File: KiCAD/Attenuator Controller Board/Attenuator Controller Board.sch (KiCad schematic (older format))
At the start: 33 parts, among them J1 Barrel_Jack_Switch, J2 Conn_Coaxial, J3 Conn_Coaxial, J4 Conn_01x24_Female, J5 DSub_15_HD, J6 DSub9, J7 DSub9, J8 DSub9, J9 Conn_01x24_Female, U1 ADM3307EARUZ, U2 ZXMHC3A01T8TA, U3 Teensy3.6

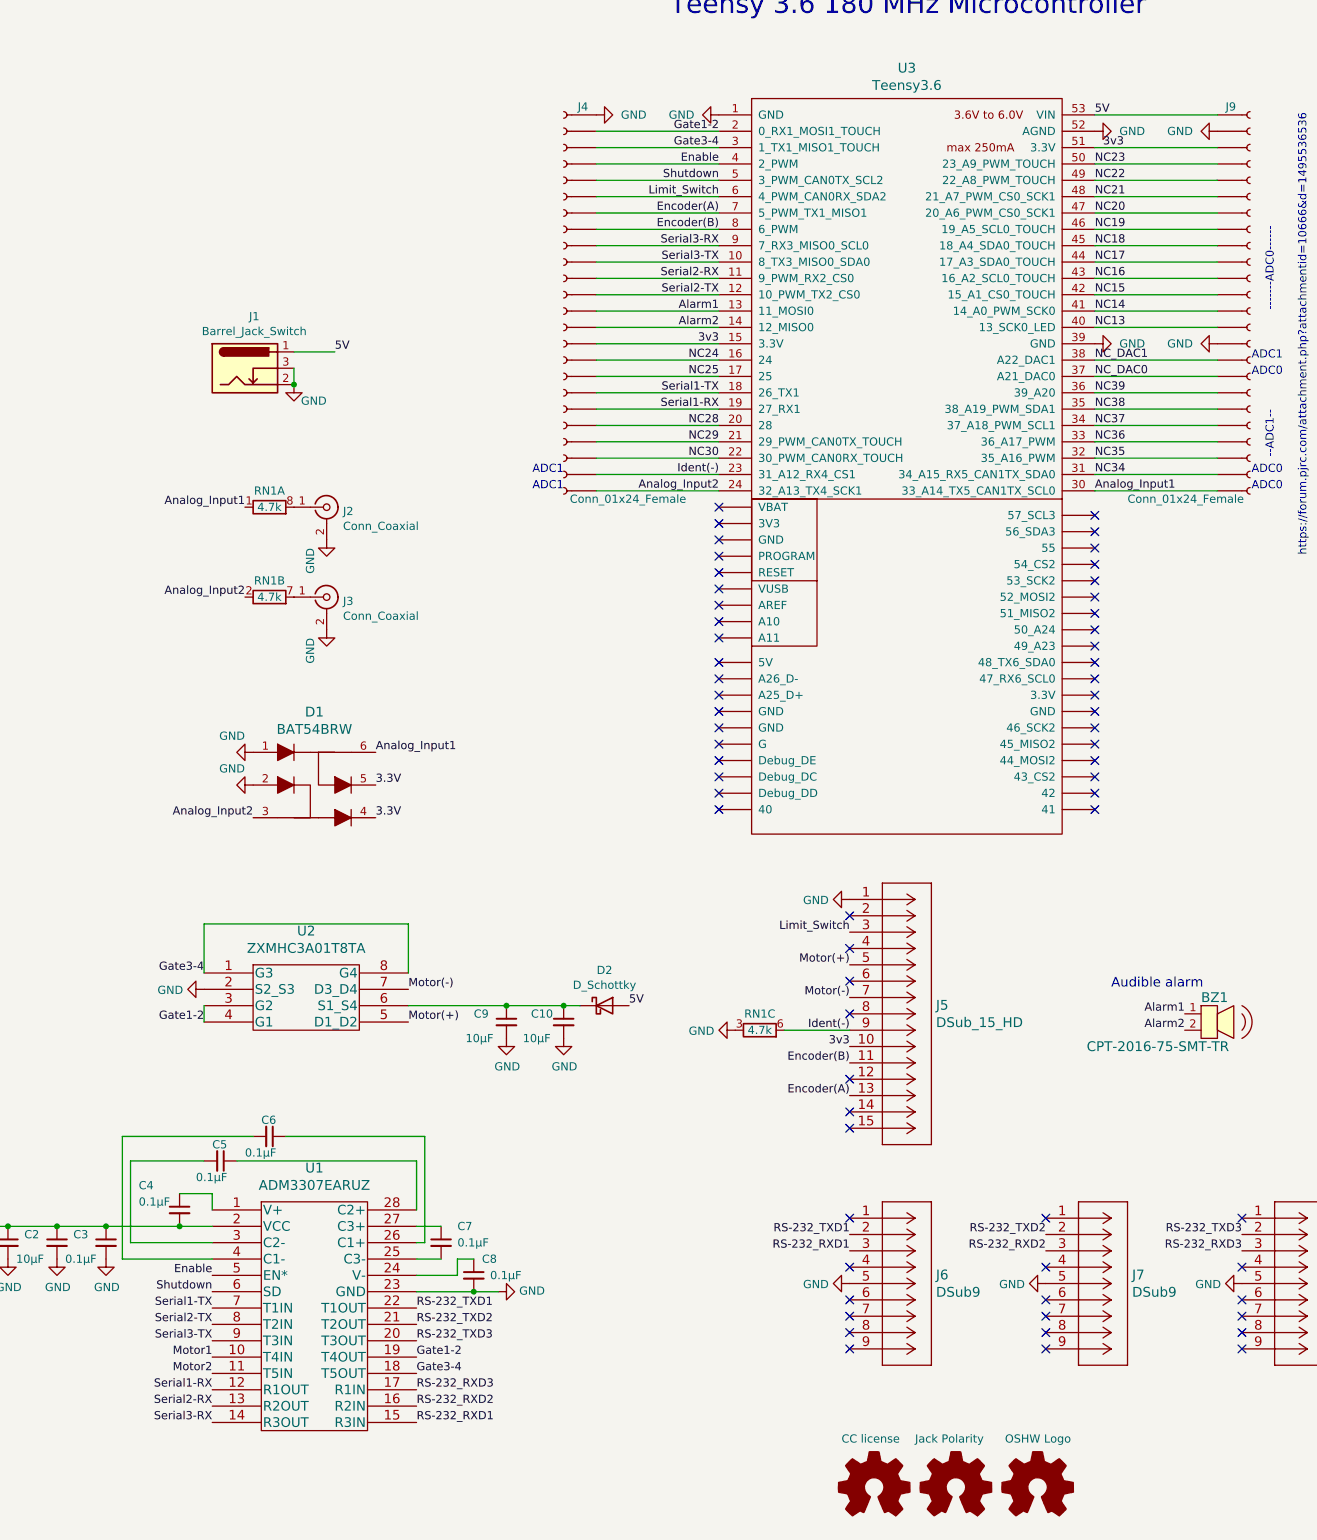
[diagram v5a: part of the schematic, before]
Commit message: Keep SD and EN low to keep RS-232 driver always on
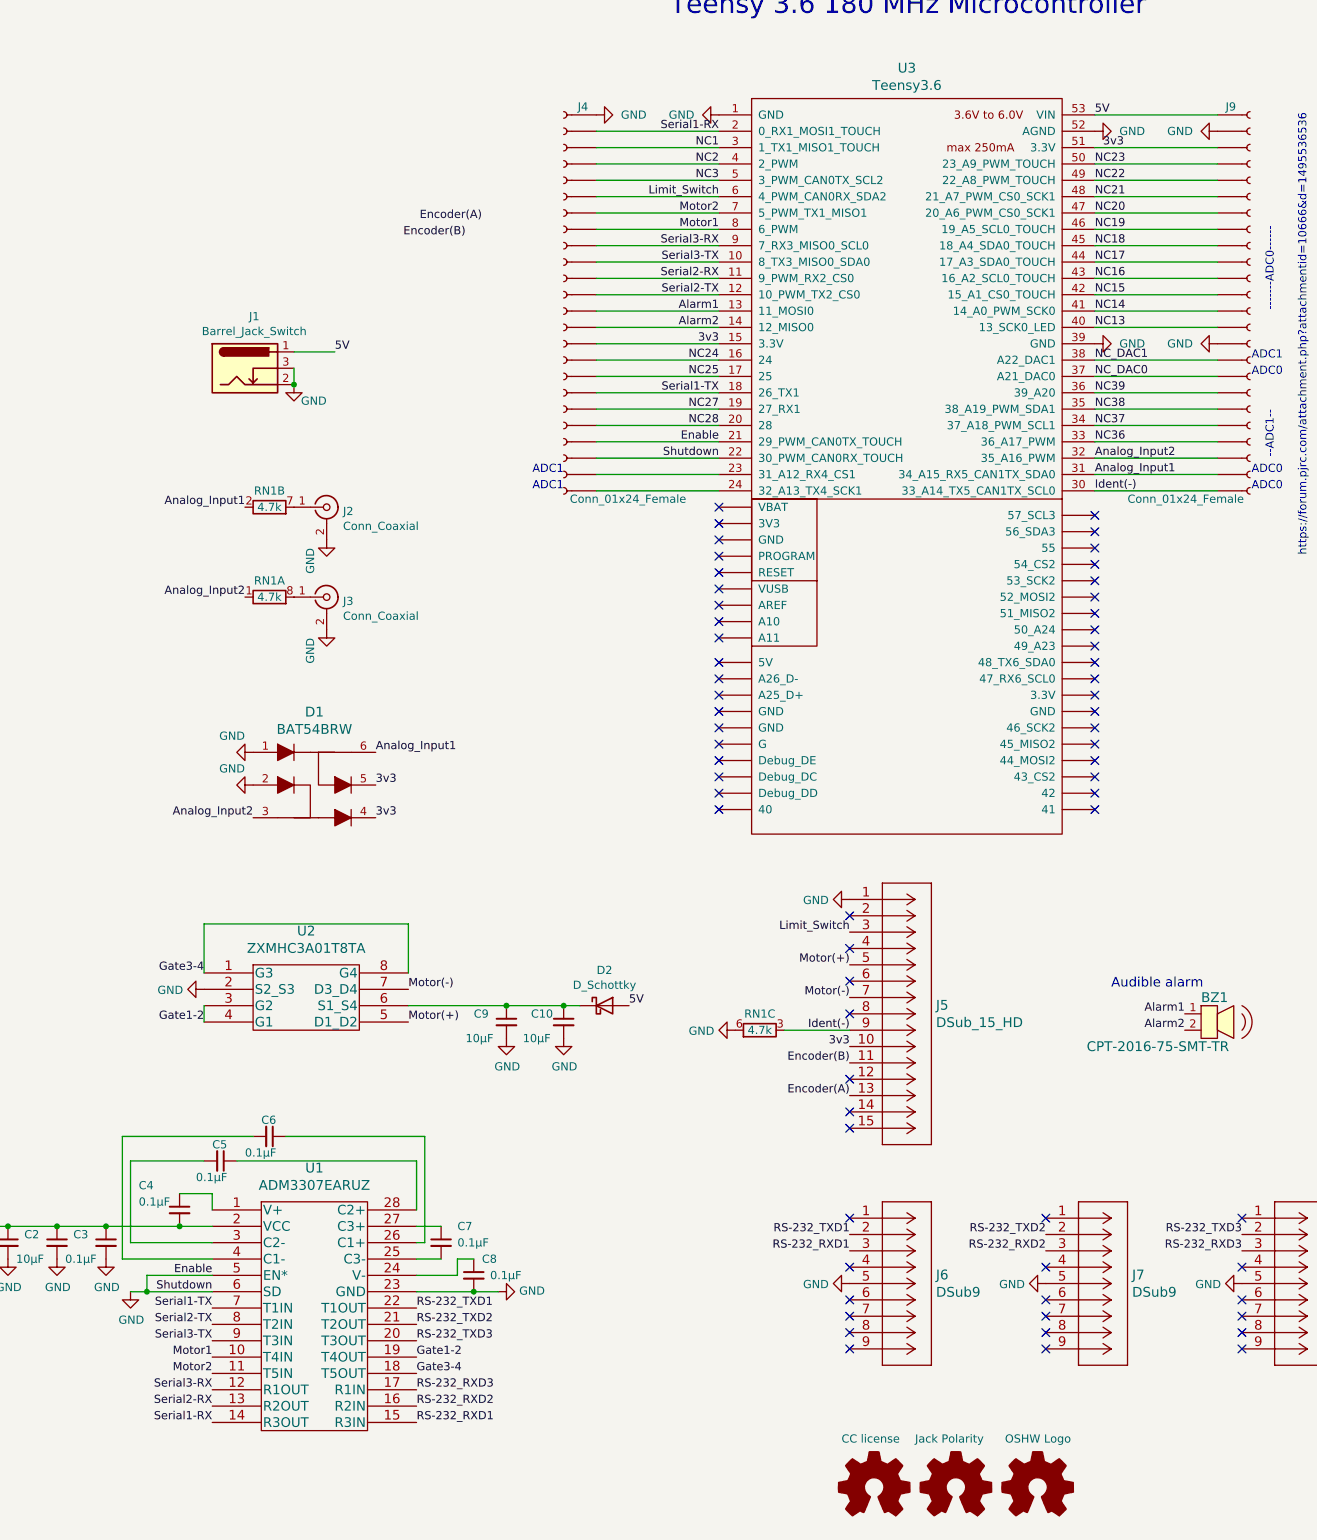
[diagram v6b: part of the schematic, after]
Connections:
- net 3.3V is gone; now on net 3v3: D1.4, D1.5
- net Analog_Input1: now also RN1.2 (R2.1), U3.31 (34_A15_RX5_CAN1TX_SDA0); no longer RN1.1 (R1.1), U3.30 (33_A14_TX5_CAN1TX_SCL0)
- net Analog_Input2: now also J9.~, RN1.1 (R1.1), U3.32 (35_A16_PWM); no longer J4.~, RN1.2 (R2.1), U3.24 (32_A13_TX4_SCK1)
- net Encoder(A): no longer J4.~, U3.7 (5_PWM_TX1_MISO1)
- net Encoder(B): no longer J4.~, U3.8 (6_PWM)
- net GND: now also RN1.6 (R3.2), U1.5 (EN*), U1.6 (SD), U3.21 (29_PWM_CAN0TX_TOUCH), U3.22 (30_PWM_CAN0RX_TOUCH); no longer RN1.3 (R3.1)
- net Gate1-2: no longer J4.~, U3.2 (0_RX1_MOSI1_TOUCH)
- net Gate3-4: no longer J4.~, U3.3 (1_TX1_MISO1_TOUCH)
- net Ident(-): now also J9.~, RN1.3 (R3.1), U3.30 (33_A14_TX5_CAN1TX_SCL0); no longer J4.~, RN1.6 (R3.2), U3.23 (31_A12_RX4_CS1)
- net Motor1: now also J4.~, U3.8 (6_PWM)
- net Motor2: now also J4.~, U3.7 (5_PWM_TX1_MISO1)
- net Serial1-RX: now also U1.14 (R3OUT), U3.2 (0_RX1_MOSI1_TOUCH); no longer U1.12 (R1OUT), U3.19 (27_RX1)
- net Serial3-RX: now also U1.12 (R1OUT); no longer U1.14 (R3OUT)
- net at J2.1 (In): now also RN1.7 (R2.2); no longer RN1.8 (R1.2)
- net at J3.1 (In): now also RN1.8 (R1.2); no longer RN1.7 (R2.2)
- removed net Enable: J4.~, U1.5 (EN*), U3.4 (2_PWM)
- removed net NC29: J4.~, U3.21 (29_PWM_CAN0TX_TOUCH)
- removed net NC30: J4.~, U3.22 (30_PWM_CAN0RX_TOUCH)
- removed net NC34: J9.~, U3.31 (34_A15_RX5_CAN1TX_SDA0)
- removed net NC35: J9.~, U3.32 (35_A16_PWM)
- removed net Shutdown: J4.~, U1.6 (SD), U3.5 (3_PWM_CAN0TX_SCL2)
- new net: J4.~, U3.23 (31_A12_RX4_CS1)
- new net: J4.~, U3.24 (32_A13_TX4_SCK1)
- new net NC1: J4.~, U3.3 (1_TX1_MISO1_TOUCH)
- new net NC2: J4.~, U3.4 (2_PWM)
- new net NC27: J4.~, U3.19 (27_RX1)
- new net NC3: J4.~, U3.5 (3_PWM_CAN0TX_SCL2)
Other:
- moved on the sheet: RN1A, RN1B
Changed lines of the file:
@@
 Text Label 13850 1500 0    50   ~ 0
 3v3
-Text Label 11500 3100 2    50   ~ 0
-Serial1-RX
 Text Label 11500 3000 2    50   ~ 0
 Serial1-TX
@@
 Text Label 8400 8600 2    50   ~ 0
 Serial1-TX
-Text Label 8400 9100 2    50   ~ 0
+Text Label 8400 9300 2    50   ~ 0
 Serial1-RX
 Text Label 11500 2300 2    50   ~ 0
@@
 Text Label 10950 6750 0    50   ~ 0
 5V
-Text Label 11500 1400 2    50   ~ 0
-Gate1-2
-Text Label 11500 1500 2    50   ~ 0
-Gate3-4
 Text Label 8350 6850 2    50   ~ 0
 Gate1-2
@@
 Text Label 9650 9100 0    50   ~ 0
 RS-232_RXD3
-Text Label 8400 9300 2    50   ~ 0
+Text Label 8400 9100 2    50   ~ 0
 Serial3-RX
 NoConn ~ 14700 8850
@@
 Text Label 8400 8500 2    50   ~ 0
 Shutdown
-Text Label 11500 1600 2    50   ~ 0
+Text Label 11500 3300 2    50   ~ 0
 Enable
-Text Label 11500 1700 2    50   ~ 0
+Text Label 11500 3400 2    50   ~ 0
 Shutdown
 Text Label 11500 1800 2    50   ~ 0
 Limit_Switch
-Text Label 11500 1900 2    50   ~ 0
+Text Label 10050 1950 2    50   ~ 0
 Encoder(A)
-Text Label 11500 2000 2    50   ~ 0
+Text Label 9950 2050 2    50   ~ 0
 Encoder(B)
 Text Label 12300 6500 2    50   ~ 0
@@
 	0    1    1    0
 $EndComp
-Text Label 11500 3500 2    50   ~ 0
+Text Label 13800 3600 0    50   ~ 0
 Ident(-)
 $Comp
@@
 $EndComp
 Text Label 9400 5400 0    50   ~ 0
-3.3V
+3v3
 Wire Wire Line
 	8900 2850 8900 2950
@@
 5V
 Text Label 9400 5600 0    50   ~ 0
-3.3V
+3v3
 $Comp
 L power:GND #PWR06
@@
 Text Label 8650 5600 2    50   ~ 0
 Analog_Input2
-Text Label 13800 3600 0    50   ~ 0
+Text Label 13800 3500 0    50   ~ 0
 Analog_Input1
-Text Label 11500 3600 2    50   ~ 0
+Text Label 13800 3400 0    50   ~ 0
 Analog_Input2
 $Comp
@@
 L Device:R_Pack04_Split RN1
 U 1 1 61FBFC7D
+P 8750 4250
+F 0 "RN1" V 8650 4250 50  0000 C CNN
+F 1 "4.7k" V 8750 4250 50  0000 C CNN
+F 2 "Resistor_SMD:R_Array_Convex_4x1206" V 8670 4250 50  0001 C CNN
+F 3 "https://industrial.panasonic.com/cdbs/www-data/pdf/AOC0000/AOC0000C14.pdf" H 8750 4250 50  0001 C CNN
+F 4 "Panasonic Electronic Components" V 8750 4250 50  0001 C CNN "Manufacturer"
+F 5 "EXB-38V472JV" V 8750 4250 50  0001 C CNN "Part #"
+	1    8750 4250
+	0    1    1    0
+$EndComp
+$Comp
+L Device:R_Pack04_Split RN1
+U 2 1 61FC4641
 P 8750 3700
 F 0 "RN1" V 8650 3700 50  0000 C CNN
@@
 F 4 "Panasonic Electronic Components" V 8750 3700 50  0001 C CNN "Manufacturer"
 F 5 "EXB-38V472JV" V 8750 3700 50  0001 C CNN "Part #"
-	1    8750 3700
-	0    1    1    0
-$EndComp
-$Comp
-L Device:R_Pack04_Split RN1
-U 2 1 61FC4641
-P 8750 4250
-F 0 "RN1" V 8650 4250 50  0000 C CNN
-F 1 "4.7k" V 8750 4250 50  0000 C CNN
-F 2 "Resistor_SMD:R_Array_Convex_4x1206" V 8670 4250 50  0001 C CNN
-F 3 "https://industrial.panasonic.com/cdbs/www-data/pdf/AOC0000/AOC0000C14.pdf" H 8750 4250 50  0001 C CNN
-F 4 "Panasonic Electronic Components" V 8750 4250 50  0001 C CNN "Manufacturer"
-F 5 "EXB-38V472JV" V 8750 4250 50  0001 C CNN "Part #"
-	2    8750 4250
+	2    8750 3700
 	0    1    1    0
 $EndComp
@@
 F 5 "EXB-38V472JV" V 11750 6900 50  0001 C CNN "Part #"
 	3    11750 6900
-	0    1    1    0
+	0    -1   1    0
 $EndComp
 $Comp
@@
 Text Label 11500 3200 2    50   ~ 0
 NC28
-Text Label 11500 3300 2    50   ~ 0
-NC29
-Text Label 11500 3400 2    50   ~ 0
-NC30
 Text Label 13800 1600 0    50   ~ 0
 NC23
@@
 Text Label 13800 3300 0    50   ~ 0
 NC36
-Text Label 13800 3400 0    50   ~ 0
-NC35
-Text Label 13800 3500 0    50   ~ 0
-NC34
 $Comp
 L Device:C_Small C10
@@
 	1    0    0    -1
 $EndComp
+Text Label 11500 2000 2    50   ~ 0
+Motor1
+Text Label 11500 1900 2    50   ~ 0
+Motor2
+Text Label 11500 1400 2    50   ~ 0
+Serial1-RX
+Text Label 11500 3100 2    50   ~ 0
+NC27
+Text Label 11500 1500 2    50   ~ 0
+NC1
+Text Label 11500 1600 2    50   ~ 0
+NC2
+Text Label 11500 1700 2    50   ~ 0
+NC3
+Wire Wire Line
+	8400 8500 8000 8500
+Wire Wire Line
+	8400 8400 8000 8400
+Wire Wire Line
+	8000 8400 8000 8500
+$Comp
+L power:GND #PWR0103
+U 1 1 61E59326
+P 7900 8500
+F 0 "#PWR0103" H 7900 8250 50  0001 C CNN
+F 1 "GND" H 7905 8327 50  0000 C CNN
+F 2 "" H 7900 8500 50  0001 C CNN
+F 3 "" H 7900 8500 50  0001 C CNN
+	1    7900 8500
+	1    0    0    -1
+$EndComp
+Wire Wire Line
+	8000 8500 7900 8500
+Connection ~ 8000 8500
 $EndSCHEMATC

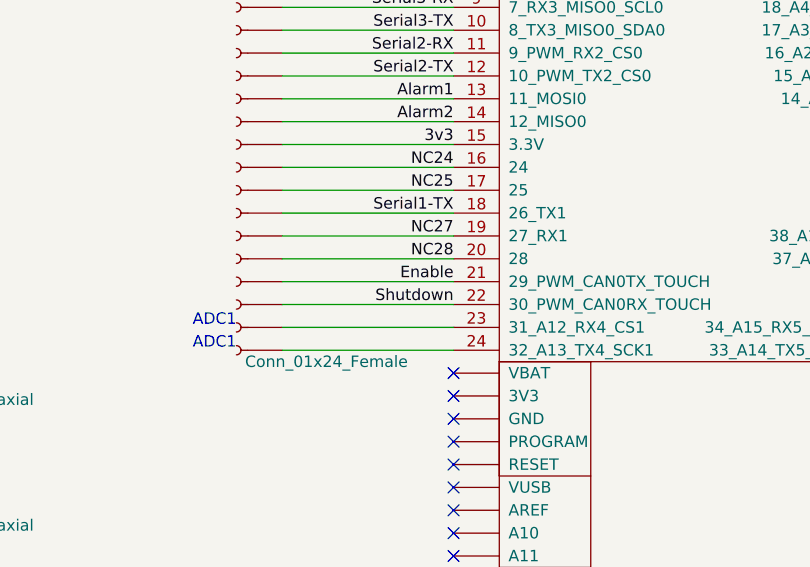
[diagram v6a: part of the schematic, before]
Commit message: Disconnect SD and EN from Teensy
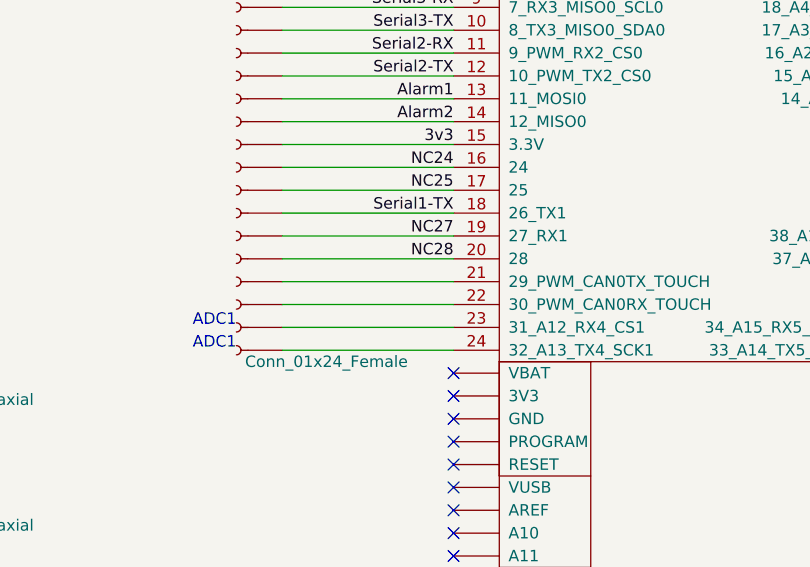
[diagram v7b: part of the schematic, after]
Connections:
- net GND: no longer U3.21 (29_PWM_CAN0TX_TOUCH), U3.22 (30_PWM_CAN0RX_TOUCH)
- new net: J4.~, U3.21 (29_PWM_CAN0TX_TOUCH)
- new net: J4.~, U3.22 (30_PWM_CAN0RX_TOUCH)
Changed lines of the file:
@@
 Text Label 8400 8500 2    50   ~ 0
-Shutdown
-Text Label 11500 3300 2    50   ~ 0
-Enable
-Text Label 11500 3400 2    50   ~ 0
 Shutdown
 Text Label 11500 1800 2    50   ~ 0

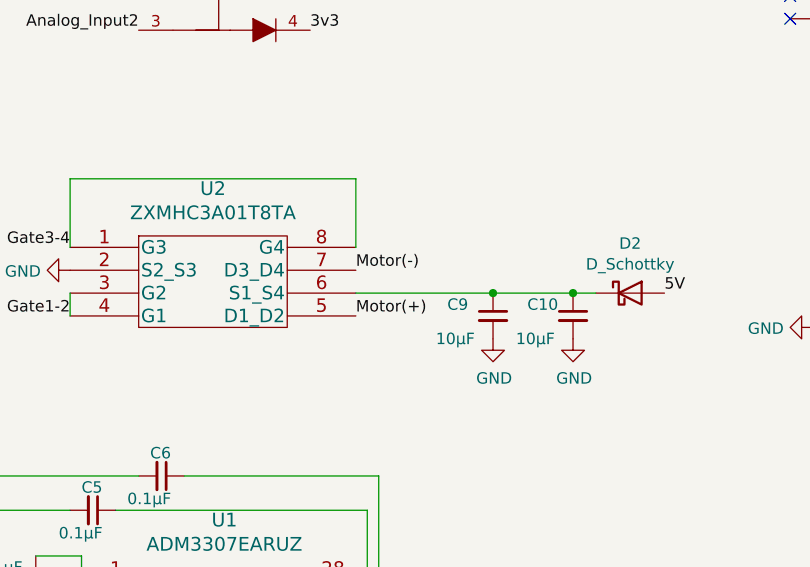
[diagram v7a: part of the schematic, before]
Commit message: Started on Thorlabs connections
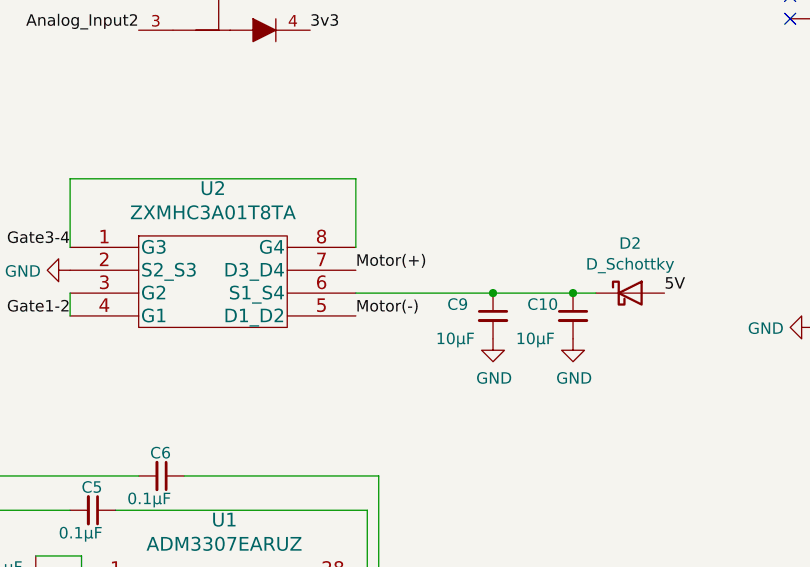
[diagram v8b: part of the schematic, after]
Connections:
- net Motor(+): now also U2.7 (D3_D4); no longer U2.5 (D1_D2)
- net Motor(-): now also U2.5 (D1_D2); no longer U2.7 (D3_D4)
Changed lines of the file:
@@
 Text Label 12300 6300 2    50   ~ 0
 Limit_Switch
-Text Label 9600 6850 0    50   ~ 0
+Text Label 9600 6650 0    50   ~ 0
 Motor(+)
 Text Label 12300 6700 2    50   ~ 0
@@
 	0    1    1    0
 $EndComp
-Text Label 9600 6650 0    50   ~ 0
+Text Label 9600 6850 0    50   ~ 0
 Motor(-)
 Text Label 10950 6750 0    50   ~ 0
